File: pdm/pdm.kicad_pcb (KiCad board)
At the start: 4 copper layers, 129.5 x 91.4 mm, 113 parts, among them J1 Conn_01x04_Male, J2 Conn_01x12_Male, J3 Conn_01x04_Female, J4 Conn_01x06_Female, M1 Fan, M2 Fan, Q1 BC817, Q10 Q_NPN_BCE, Q11 Q_PMOS_DSG, Q2 Q_NPN_BCE, Q3 BC817, Q4 Q_NPN_BCE, Q5 BC817, Q6 Q_NPN_BCE, Q7 BC817, Q8 Q_NPN_BCE, Q9 BC817, SW1 SW_Push, U1 LM2937xS, U2 SN65HVD233, U3 STM32F042G6Ux, U4 BTS443P, U5 BTS443P, U6 BTS443P, U7 BTS443P, U8 BTS443P

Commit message: fixed DRC's
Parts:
- J3: footprint Connector_PinHeader_2.54mm:PinHeader_1x04_P2.54mm_Vertical_SMD_Pin1Left -> Connector_PinSocket_2.54mm:PinSocket_1x04_P2.54mm_Vertical_SMD_Pin1Left
- J4: footprint Connector_PinHeader_2.54mm:PinHeader_1x06_P2.54mm_Vertical_SMD_Pin1Left -> Connector_PinSocket_2.54mm:PinSocket_1x06_P2.54mm_Vertical_SMD_Pin1Left
- moved C3 4.83 mm to (116.5, 67.1)
- moved C6 2.03 mm to (133.5, 66.6)
- moved R2 1.80 mm to (172.1, 66.1)
- moved C5 0.36 mm to (168.3, 62.1)
- moved C8 0.13 mm to (165.0, 56.0)
- turned TP9 to 0 degrees
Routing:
- net +12V: track 19.1 -> 21.4 mm
- net /NRST: track 20.4 -> 22.3 mm, vias 2 -> 1
- net /act5: track 70.3 -> 69.2 mm
- net /act4: track 45.3 -> 44.3 mm
- net /fuse5: track 97.0 -> 96.0 mm
- net /fuse4: track 72.6 -> 71.6 mm
- net GND: track 17.4 -> 18.4 mm, vias 87 -> 125
- net +3V3: track 104.7 -> 104.9 mm, vias 30 -> 13
- net /_P: vias 0 -> 1
- net /_N: vias 0 -> 1

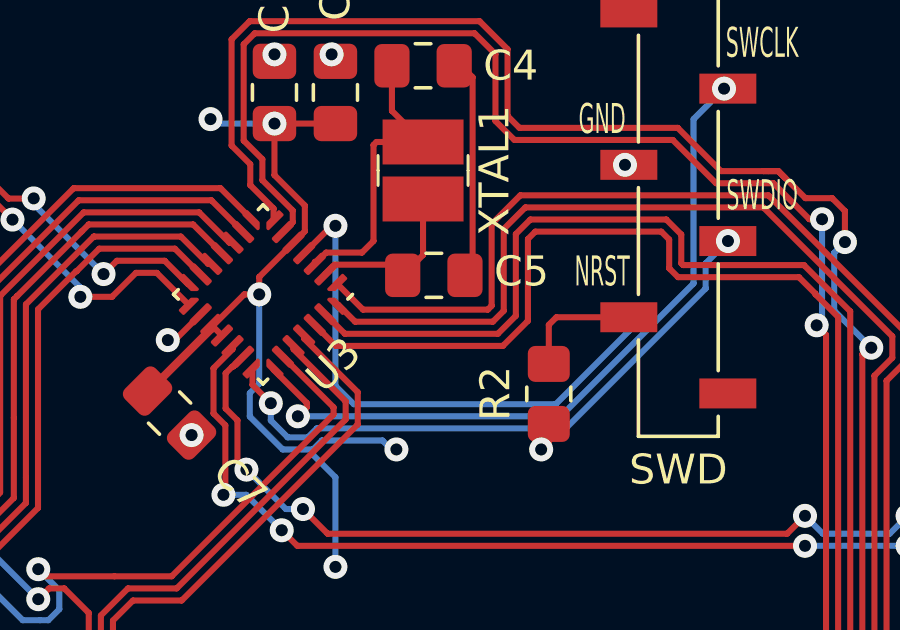
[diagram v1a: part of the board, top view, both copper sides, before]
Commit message: added nrst conenction
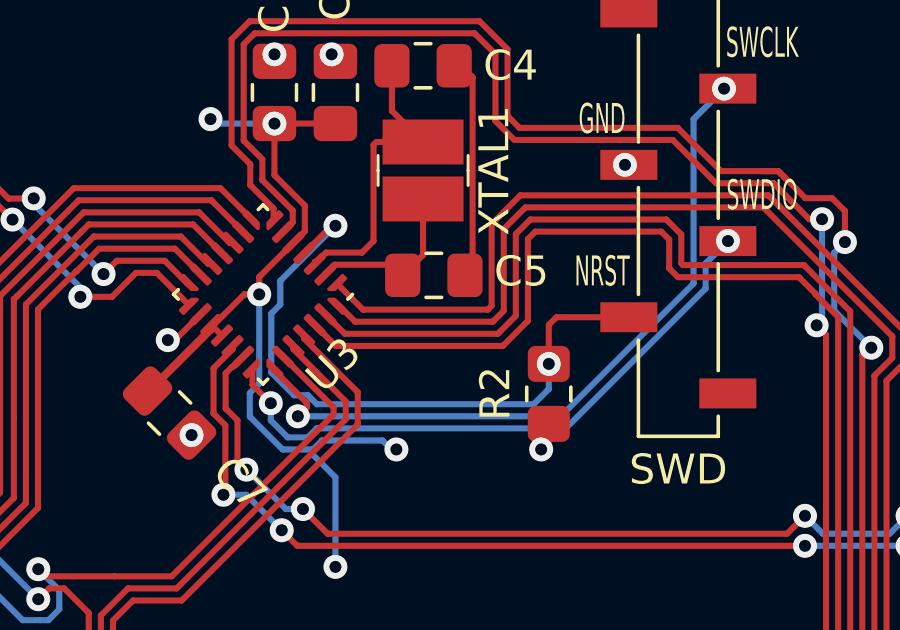
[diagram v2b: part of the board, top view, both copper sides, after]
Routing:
- net /NRST: track 22.3 -> 22.0 mm, vias 1 -> 2
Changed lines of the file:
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@@
     (thickness 1.6)
     (drawings 118)
-    (tracks 1491)
+    (tracks 1497)
     (zones 0)
     (modules 113)
@@
   )
   (setup
-    (last_trace_width 1)
+    (last_trace_width 0.2032)
     (user_trace_width 0.2032)
     (user_trace_width 0.254)
@@
   (via (at 133.304 65.197) (size 0.8) (drill 0.4) (layers F.Cu B.Cu) (net 3))
   (segment (start 133.477 65.197) (end 133.304 65.197) (width 1) (layer F.Cu) (net 3))
-  (via (at 164.973 60.452) (size 0.8) (drill 0.4) (layers F.Cu B.Cu) (net 4))
-  (segment (start 164.846 60.452) (end 163.930019 61.367981) (width 0.2032) (layer F.Cu) (net 4))
-  (segment (start 164.973 60.452) (end 164.846 60.452) (width 0.2032) (layer F.Cu) (net 4))
-  (segment (start 164.973 60.452) (end 164.973 65.786) (width 0.2032) (layer B.Cu) (net 4))
-  (segment (start 164.973 65.786) (end 165.58579 66.39879) (width 0.2032) (layer B.Cu) (net 4))
-  (segment (start 165.58579 66.39879) (end 172.317356 66.39879) (width 0.2032) (layer B.Cu) (net 4))
-  (segment (start 174.748 63.968146) (end 174.748 63.5) (width 0.2032) (layer B.Cu) (net 4))
-  (segment (start 172.317356 66.39879) (end 174.748 63.968146) (width 0.2032) (layer B.Cu) (net 4))
   (segment (start 172.085 65.056) (end 172.085 63.754) (width 0.2032) (layer F.Cu) (net 4))
   (segment (start 172.339 63.5) (end 174.753 63.5) (width 0.2032) (layer F.Cu) (net 4))
   (segment (start 172.085 63.754) (end 172.339 63.5) (width 0.2032) (layer F.Cu) (net 4))
+  (via (at 172.085 65.056) (size 0.8) (drill 0.4) (layers F.Cu B.Cu) (net 4))
+  (via (at 164.973 60.452) (size 0.8) (drill 0.4) (layers F.Cu B.Cu) (net 4))
+  (segment (start 164.846 60.452) (end 163.930019 61.367981) (width 0.2032) (layer F.Cu) (net 4))
+  (segment (start 164.973 60.452) (end 164.846 60.452) (width 0.2032) (layer F.Cu) (net 4))
+  (segment (start 162.83621 65.344507) (end 162.83621 63.37316) (width 0.2032) (layer B.Cu) (net 4))
+  (segment (start 162.83621 63.37316) (end 163.134601 63.074769) (width 0.2032) (layer B.Cu) (net 4))
+  (segment (start 163.592102 66.100399) (end 162.83621 65.344507) (width 0.2032) (layer B.Cu) (net 4))
+  (segment (start 164.055749 66.100399) (end 163.592102 66.100399) (width 0.2032) (layer B.Cu) (net 4))
+  (segment (start 164.35414 66.39879) (end 164.055749 66.100399) (width 0.2032) (layer B.Cu) (net 4))
+  (segment (start 171.577 66.39879) (end 164.35414 66.39879) (width 0.2032) (layer B.Cu) (net 4))
+  (segment (start 172.085 65.89079) (end 171.577 66.39879) (width 0.2032) (layer B.Cu) (net 4))
+  (segment (start 163.134601 62.290399) (end 164.973 60.452) (width 0.2032) (layer B.Cu) (net 4))
+  (segment (start 163.134601 63.074769) (end 163.134601 62.290399) (width 0.2032) (layer B.Cu) (net 4))
+  (segment (start 172.085 65.056) (end 172.085 65.89079) (width 0.2032) (layer B.Cu) (net 4))
   (segment (start 162.911786 65.211106) (end 162.911786 65.248786) (width 0.2032) (layer F.Cu) (net 5))
   (segment (start 162.911786 65.248786) (end 164.01737 66.35437) (width 0.2032) (layer F.Cu) (net 5))

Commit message: added fixes for issue #11 #12 & #13
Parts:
- removed Q11: Q_PMOS_DSG, Package_TO_SOT_SMD:TO-252-2
- added D9: D, digikey-footprints:DO-214AB, F.Cu at (157.2, 119.9)
- added Q12: BC817, Package_TO_SOT_SMD:SOT-23, F.Cu at (157.0, 105.6)
- added Q13: BC817, Package_TO_SOT_SMD:SOT-23, F.Cu at (181.6, 105.7)
- added Q14: BC817, Package_TO_SOT_SMD:SOT-23, F.Cu at (205.9, 106.0)
- added Q15: BC817, Package_TO_SOT_SMD:SOT-23, F.Cu at (107.6, 105.4)
- added Q16: BC817, Package_TO_SOT_SMD:SOT-23, F.Cu at (132.2, 105.4)
- added R42: 10k, Resistor_SMD:R_0805_2012Metric_Pad1.20x1.40mm_HandSolder, F.Cu at (156.9, 102.7)
- added R43: 10k, Resistor_SMD:R_0805_2012Metric_Pad1.20x1.40mm_HandSolder, F.Cu at (181.5, 102.8)
- added R44: 10k, Resistor_SMD:R_0805_2012Metric_Pad1.20x1.40mm_HandSolder, F.Cu at (205.7, 103.1)
- added R45: 10k, Resistor_SMD:R_0805_2012Metric_Pad1.20x1.40mm_HandSolder, F.Cu at (107.4, 102.5)
- added R46: 10k, Resistor_SMD:R_0805_2012Metric_Pad1.20x1.40mm_HandSolder, F.Cu at (132.1, 102.5)
- C3: value 0.1u -> 0.1uF
- Q10, Q2, Q4, Q6, Q8: value Q_NPN_BCE -> BC817; footprint Package_TO_SOT_SMD:SOT-23_Handsoldering -> Package_TO_SOT_SMD:SOT-23
- R10, R17, R24, R31, R38: value 680 -> 680R
- R2, R5: value 10K -> 10k
- moved R10 18.0 mm to (133.0, 99.5), turned to 90 degrees
- moved R24 18.0 mm to (157.8, 99.6), turned to 90 degrees
- moved R38 18.0 mm to (206.6, 100.1), turned to 90 degrees
- moved R17 18.0 mm to (108.3, 99.5), turned to 90 degrees
- moved R31 18.0 mm to (182.4, 99.8), turned to 90 degrees
- moved M1 1.77 mm to (218.1, 117.1)
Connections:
- D4 pad 1: GND -> Net-(D4-Pad1)
- D5 pad 1: GND -> Net-(D5-Pad1)
- D6 pad 1: GND -> Net-(D6-Pad1)
- D7 pad 1: GND -> Net-(D7-Pad1)
- D8 pad 1: GND -> Net-(D8-Pad1)
- J1 pad 2: /vin -> +12V
- J1 pad 3: /vin -> +12V
- J1 pad 4: /vin -> +12V
- R10 pad 1: /vout2 -> /act2
- R17 pad 1: /vout1 -> /act1
- R24 pad 1: /vout3 -> /act3
- R31 pad 1: /vout4 -> /act4
- R38 pad 1: /vout5 -> /act5
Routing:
- net /act4: track 44.3 -> 70.5 mm
- net /act2: track 54.6 -> 80.7 mm
- net /act1: track 76.1 -> 102.2 mm
- net /act5: track 69.2 -> 95.2 mm
- net /act3: track 27.5 -> 53.2 mm
- net Net-(D7-Pad2): track 27.3 -> 1.96 mm, vias 2 -> 0
- net Net-(D5-Pad2): track 27.1 -> 1.96 mm, vias 2 -> 0
- net Net-(D6-Pad2): track 26.3 -> 1.96 mm, vias 2 -> 0
- net Net-(D8-Pad2): track 26.2 -> 1.96 mm, vias 2 -> 0
- net Net-(D4-Pad2): track 25.8 -> 1.96 mm, vias 2 -> 0
- net /vout1: track 103.6 -> 126.4 mm, vias 0 -> 1
- net /vout5: track 205.8 -> 186.7 mm, vias 0 -> 1
- net /vout2: track 76.8 -> 90.9 mm, vias 0 -> 1
- net Net-(D7-Pad1): track 0.00 -> 12.8 mm
- net Net-(D8-Pad1): track 0.00 -> 12.8 mm
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- added copper zone on In1.Cu, net +3V3
- removed copper zone on F.Cu, net +3V3
- removed copper zone on F.Cu, net /vin

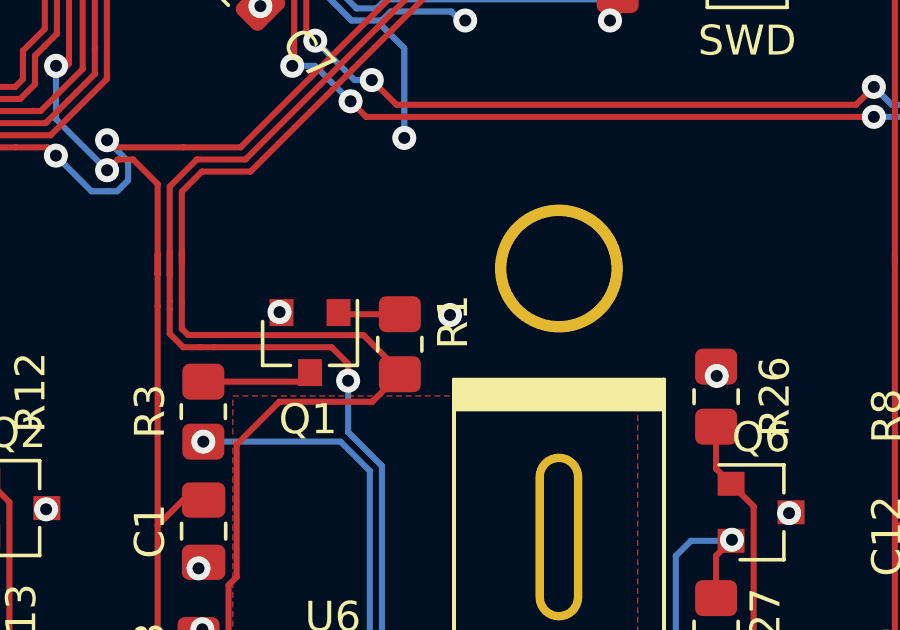
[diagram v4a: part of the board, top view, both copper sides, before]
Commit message: removed 3v3 w/ gnd on out
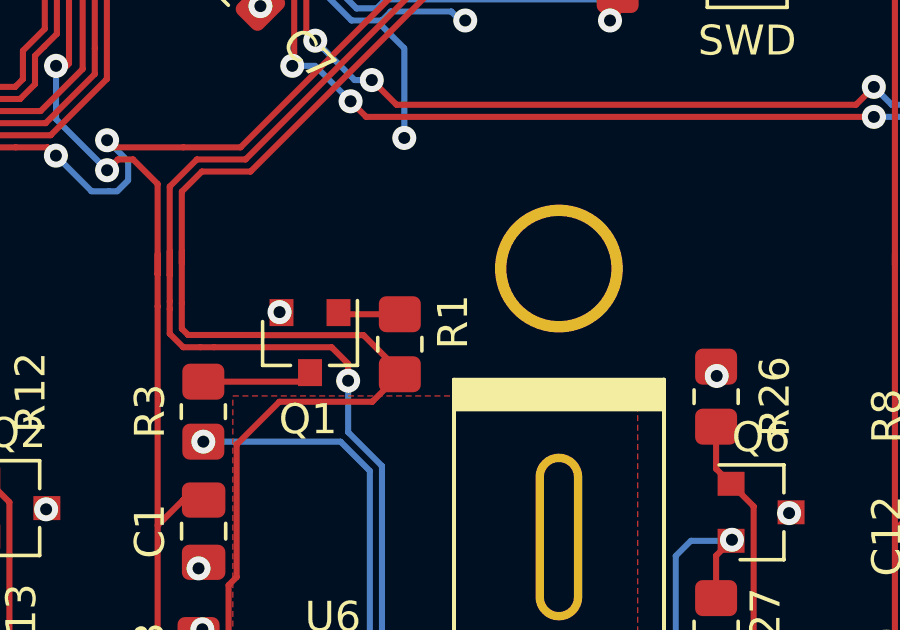
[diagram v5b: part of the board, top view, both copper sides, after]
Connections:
- J2 pad 1: +3V3 -> GND
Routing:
- net +3V3: track 106.3 -> 57.5 mm, vias 21 -> 20
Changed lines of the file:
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@@
   (general
     (thickness 1.6)
-    (drawings 118)
-    (tracks 1588)
+    (drawings 120)
+    (tracks 1583)
     (zones 0)
     (modules 123)
@@
     (fp_line (start -21.605 -9.4) (end 21.605 -9.4) (layer F.Fab) (width 0.127))
     (pad 1 thru_hole rect (at -11.115 -6.35) (size 2.715 2.715) (drill 1.81) (layers *.Cu *.Mask)
-      (net 3 +3V3))
+      (net 1 GND))
     (pad 2 thru_hole circle (at -6.67 -6.35) (size 2.715 2.715) (drill 1.81) (layers *.Cu *.Mask)
       (net 1 GND))
@@
     )
   )
+  (dimension 129.54 (width 0.15) (layer Dwgs.User)
+    (gr_text "129.540 mm" (at 169.037 36.419) (layer Dwgs.User)
+      (effects (font (size 1 1) (thickness 0.15)))
+    )
+    (feature1 (pts (xy 104.267 48.514) (xy 104.267 37.132579)))
+    (feature2 (pts (xy 233.807 48.514) (xy 233.807 37.132579)))
+    (crossbar (pts (xy 233.807 37.719) (xy 104.267 37.719)))
+    (arrow1a (pts (xy 104.267 37.719) (xy 105.393504 37.132579)))
+    (arrow1b (pts (xy 104.267 37.719) (xy 105.393504 38.305421)))
+    (arrow2a (pts (xy 233.807 37.719) (xy 232.680496 37.132579)))
+    (arrow2b (pts (xy 233.807 37.719) (xy 232.680496 38.305421)))
+  )
+  (dimension 91.44 (width 0.15) (layer Dwgs.User)
+    (gr_text "91.440 mm" (at 248.442 94.234 270) (layer Dwgs.User)
+      (effects (font (size 1 1) (thickness 0.15)))
+    )
+    (feature1 (pts (xy 233.807 139.954) (xy 247.728421 139.954)))
+    (feature2 (pts (xy 233.807 48.514) (xy 247.728421 48.514)))
+    (crossbar (pts (xy 247.142 48.514) (xy 247.142 139.954)))
+    (arrow1a (pts (xy 247.142 139.954) (xy 246.555579 138.827496)))
+    (arrow1b (pts (xy 247.142 139.954) (xy 247.728421 138.827496)))
+    (arrow2a (pts (xy 247.142 48.514) (xy 246.555579 49.640504)))
+    (arrow2b (pts (xy 247.142 48.514) (xy 247.728421 49.640504)))
+  )
   (gr_text FAN2 (at 224.917 115.57 90) (layer F.SilkS)
     (effects (font (size 1 1) (thickness 0.15)))
@@
   (segment (start 198.247 77.95837) (end 198.247 79.40599) (width 0.2032) (layer B.Cu) (net 3))
   (segment (start 199.009 77.19637) (end 198.247 77.95837) (width 0.2032) (layer B.Cu) (net 3))
-  (segment (start 167.295001 112.497001) (end 167.295001 100.323999) (width 1) (layer In1.Cu) (net 3))
-  (segment (start 167.295001 100.323999) (end 167.295001 78.522001) (width 1) (layer In1.Cu) (net 3))
-  (segment (start 167.295001 78.522001) (end 166.497 77.724) (width 1) (layer In1.Cu) (net 3))
-  (via (at 166.497 77.724) (size 0.8) (drill 0.4) (layers F.Cu B.Cu) (net 3))
-  (segment (start 176.972 122.174) (end 167.295001 112.497001) (width 1) (layer In1.Cu) (net 3))
   (via (at 129.667 72.03118) (size 0.8) (drill 0.4) (layers F.Cu B.Cu) (net 3))
   (segment (start 129.051 71.41518) (end 129.667 72.03118) (width 1) (layer In1.Cu) (net 3))

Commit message: added phatter tracks
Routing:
- net /vout3: track 166.5 -> 209.8 mm
- net /vout4: track 150.6 -> 187.9 mm
- net /vout2: track 90.9 -> 95.3 mm
- net /vout1: track 126.4 -> 125.5 mm
- net /vout5: track 186.7 -> 187.6 mm
- net GND: track 17.8 -> 18.1 mm, vias 173 -> 125

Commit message: Fixed LED Work
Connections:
- R10 pad 1: /act2 -> /vout2
- R17 pad 1: /act1 -> /vout1
- R24 pad 1: /act3 -> /vout3
- R31 pad 1: /act4 -> /vout4
- R38 pad 1: /act5 -> /vout5
- R42 pad 2: /vout3 -> /act3
- R43 pad 2: /vout4 -> /act4
- R44 pad 2: /vout5 -> /act5
- R45 pad 2: /vout1 -> /act1
- R46 pad 2: /vout2 -> /act2
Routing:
- net /act4: track 70.5 -> 74.7 mm
- net /act1: track 102.2 -> 106.2 mm
- net /act5: track 95.2 -> 99.1 mm
- net /act3: track 53.2 -> 57.0 mm
- net /act2: track 80.7 -> 84.4 mm
- net /vout4: track 187.9 -> 186.6 mm
- net /vout3: track 209.8 -> 208.6 mm
- net /vout2: track 95.3 -> 94.1 mm
- net /vout5: track 187.6 -> 186.7 mm

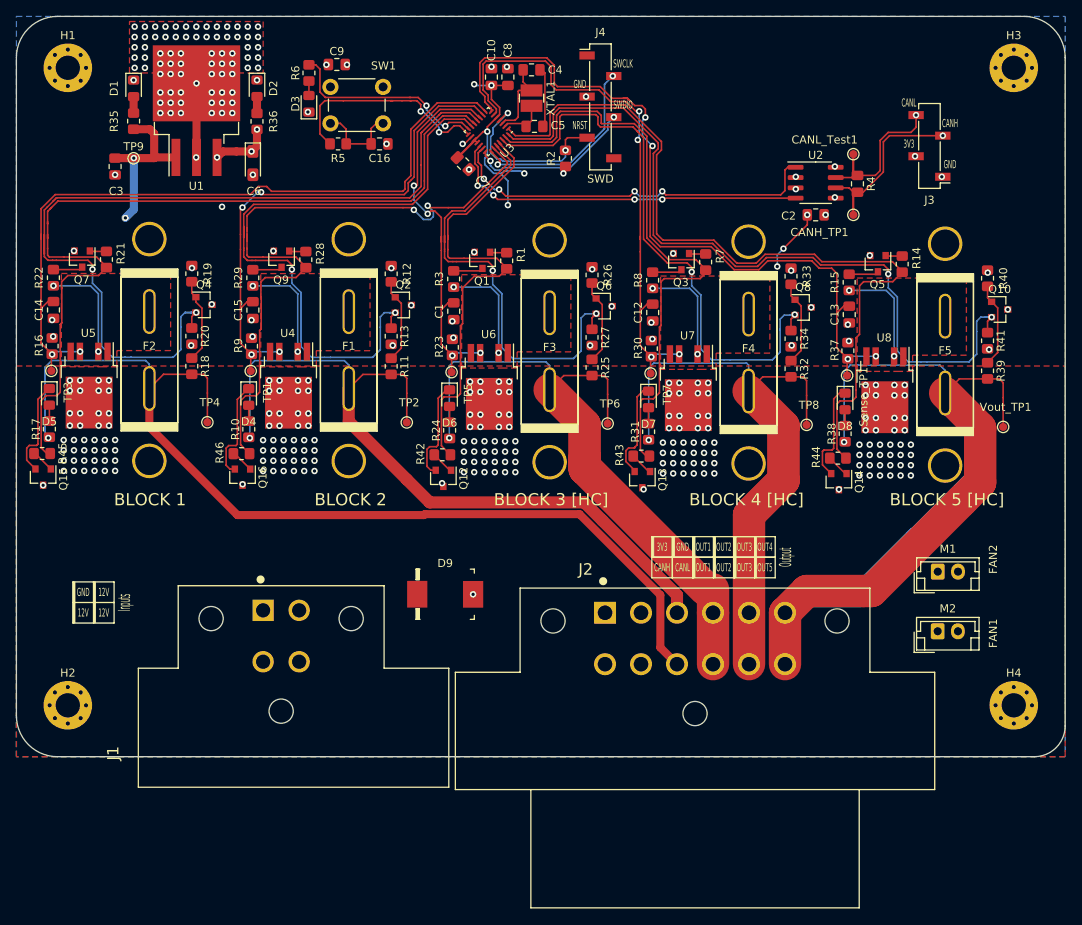
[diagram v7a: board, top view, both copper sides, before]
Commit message: changed oscilltor and exposed themral pads
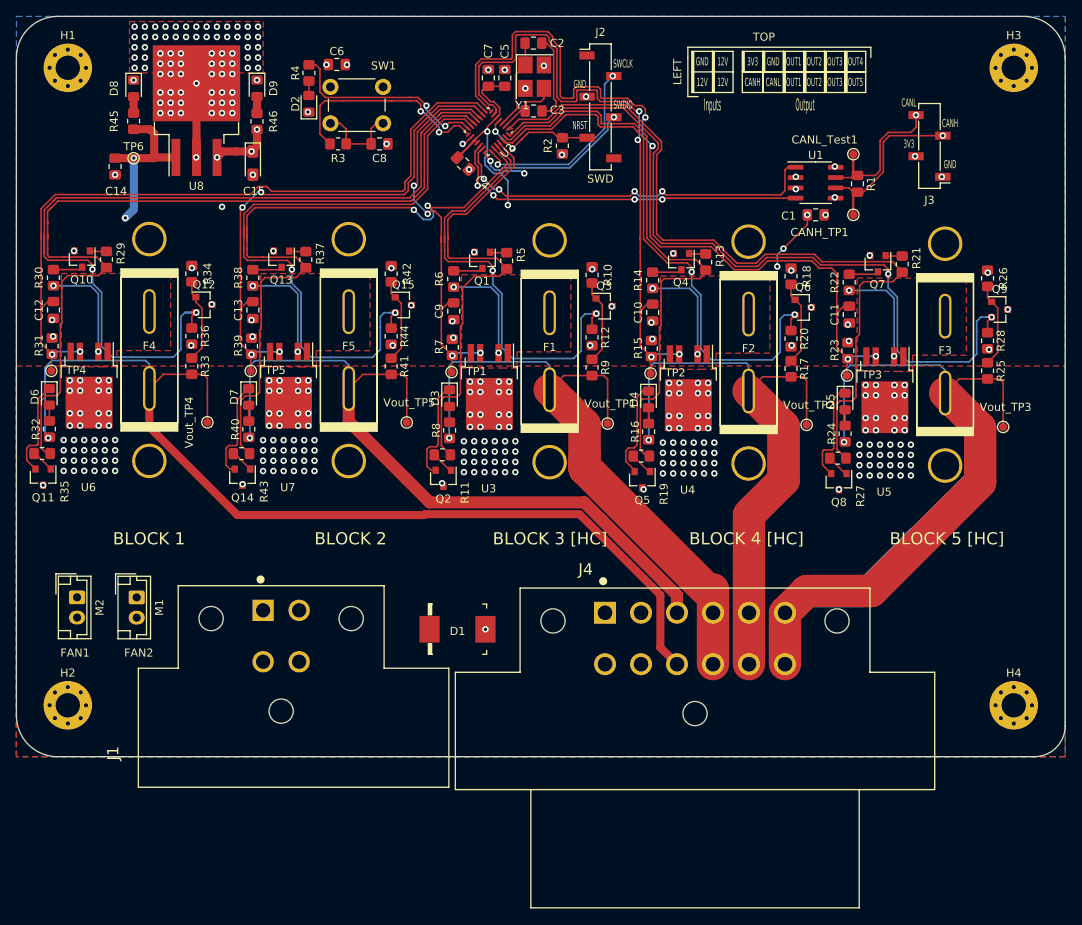
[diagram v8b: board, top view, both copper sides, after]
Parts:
- removed the C8 at (165.0, 56.0)
- removed XTAL1: NX3225GD-8MHZ-STD-CRA-3, digikey-footprints:SMD-2_3.2x2.5mm
- added C5: 1uF, Capacitor_SMD:C_0805_2012Metric_Pad1.18x1.45mm_HandSolder, F.Cu at (164.6, 56.1)
- added RarePepe1: RarePepe, pdm_v2:rarepepe, F.Cu at (142.5, 108.5)
- added Y1: Crystal_GND24, Crystal:Crystal_SMD_3225-4Pin_3.2x2.5mm_HandSoldering, F.Cu at (168.3, 56.0)
- R11: renamed from R42; value 10k -> 2k2
- R13: renamed from R7; value 2k8 -> 2k2
- R16: renamed from R31; value 680R -> 850
- R19: renamed from R43; value 10k -> 2k2
- R21: renamed from R14; value 2k8 -> 2k2
- R24: renamed from R38; value 680R -> 850
- R27: renamed from R44; value 10k -> 2k2
- R29: renamed from R21; value 2k8 -> 2k2
- R32: renamed from R17; value 680R -> 850
- R35: renamed from R45; value 10k -> 2k2
- R37: renamed from R28; value 2k8 -> 2k2
- R4: renamed from R6; value 600R -> 120R
- R40: renamed from R10; value 680R -> 850
- R43: renamed from R46; value 10k -> 2k2
- R45: renamed from R35; value 600R -> 850
- R46: renamed from R36; value 600R -> 120R
- R5: renamed from R1; value 2k8 -> 2k2
- R8: renamed from R24; value 680R -> 850
- moved M2 106.4 mm to (111.8, 120.3), turned to 270 degrees
- moved M1 99.0 mm to (119.1, 120.3), turned to 270 degrees
- moved D1 4.58 mm to (158.7, 124.2)
- moved C2 3.31 mm to (168.1, 51.8)
- moved C3 1.91 mm to (168.1, 60.2)
- moved R2 1.60 mm to (171.7, 64.5)
- moved C7 0.40 mm to (162.6, 56.1)
- renumbered C2 to C1, C12 to C10, C13 to C11, C14 to C12, C15 to C13, C3 to C14, C6 to C15, C4 to C2, C5 to C3, C7 to C4, C9 to C6, C10 to C7, C16 to C8, C1 to C9, D9 to D1, D3 to D2, D6 to D3, D7 to D4, D8 to D5, D5 to D6, D4 to D7, D1 to D8, D2 to D9, F3 to F1, F4 to F2, F5 to F3, F2 to F4, F1 to F5, J4 to J2, J2 to J4, Q7 to Q10, Q15 to Q11, Q4 to Q12, Q9 to Q13, Q16 to Q14, Q2 to Q15, Q12 to Q2, Q6 to Q3, Q3 to Q4, Q13 to Q5, Q8 to Q6, Q5 to Q7, Q14 to Q8, Q10 to Q9, R4 to R1, R26 to R10, R27 to R12, R8 to R14, R30 to R15, R32 to R17, R33 to R18, R34 to R20, R15 to R22, R37 to R23, R39 to R25, R40 to R26, R41 to R28, R5 to R3, R22 to R30, R16 to R31, R18 to R33, R19 to R34, R20 to R36, R29 to R38, R9 to R39, R11 to R41, R12 to R42, R13 to R44, R3 to R6, R23 to R7, R25 to R9, TP5 to TP1, TP7 to TP2, Sense_TP1 to TP3, TP3 to TP4, TP1 to TP5, TP9 to TP6, U2 to U1, U3 to U2, U6 to U3, U7 to U4, U8 to U5, U5 to U6, U4 to U7, U1 to U8, TP6 to Vout_TP1, TP8 to Vout_TP2, Vout_TP1 to Vout_TP3, TP4 to Vout_TP4, TP2 to Vout_TP5
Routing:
- net /sense4: track 69.4 -> 80.4 mm
- net /sense5: track 93.2 -> 102.1 mm
- net /NRST: track 22.0 -> 14.9 mm
- net Net-(C2-Pad1): track 7.63 -> 10.9 mm
- net /OSC_N: track 5.70 -> 8.09 mm
- net /fuse5: track 97.1 -> 95.0 mm
- net /fuse4: track 72.6 -> 70.7 mm
- net /act4: track 74.7 -> 72.8 mm
- net /act5: track 99.1 -> 97.3 mm
- net +3V3: track 57.5 -> 56.2 mm, vias 20 -> 18
- net GND: track 18.1 -> 17.0 mm, vias 125 -> 127
- net /OSC_P: track 10.2 -> 11.3 mm
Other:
- rule pad_to_mask_clearance: 0.05 -> 0
- board text added: "LEFT"
- board text added: "TOP"
